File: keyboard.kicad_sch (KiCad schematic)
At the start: 273 parts, among them J3 USB_C_Receptacle_USB2.0, Q1 DTC143Z, SW1 SW_Push, U1 MIC5219-3.3YMM, U3 STM32F072R8Tx, Y1 16MHz

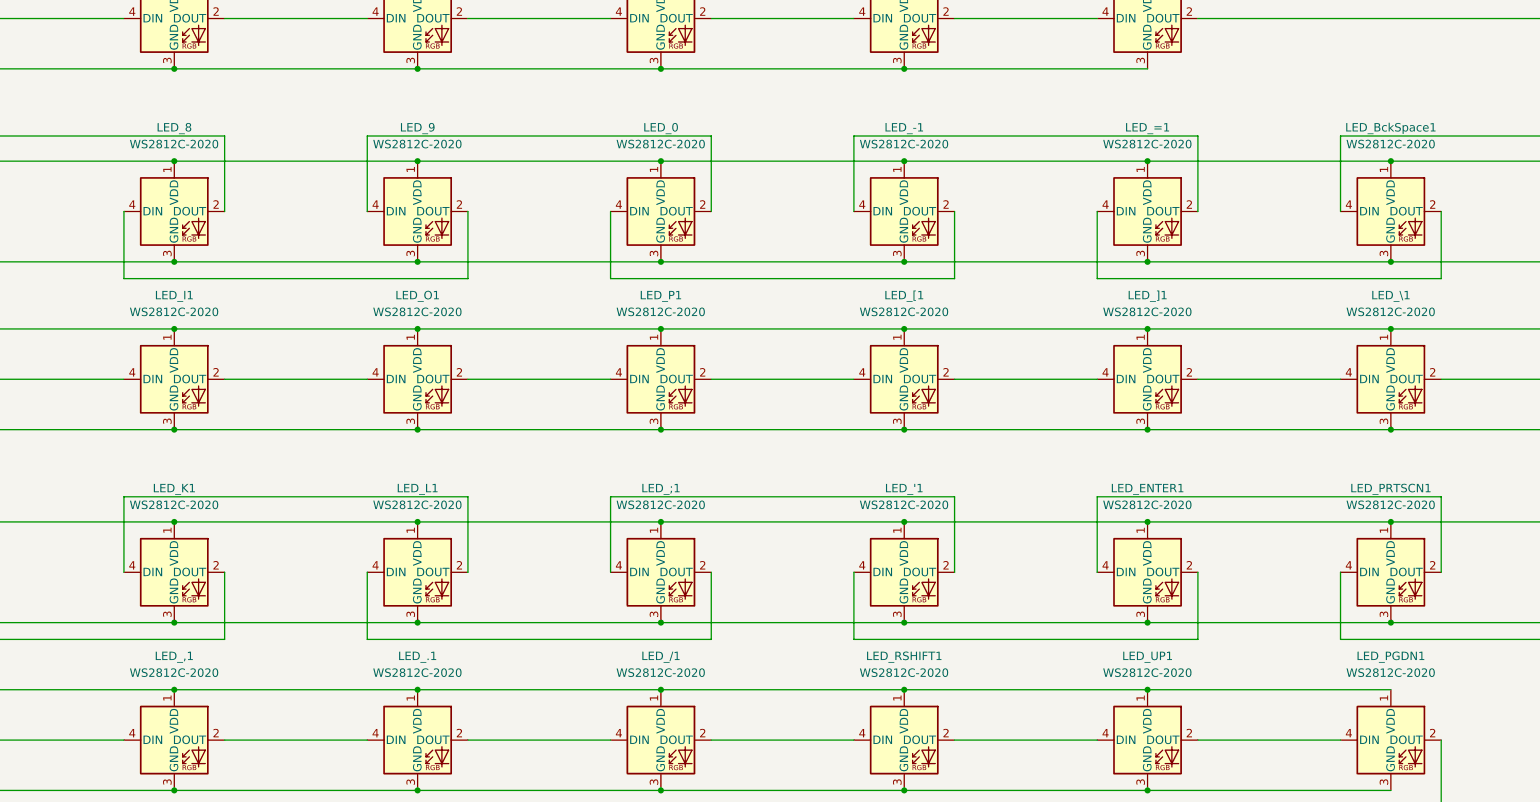
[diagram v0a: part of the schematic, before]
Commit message: fixed led for minus with custom footprint
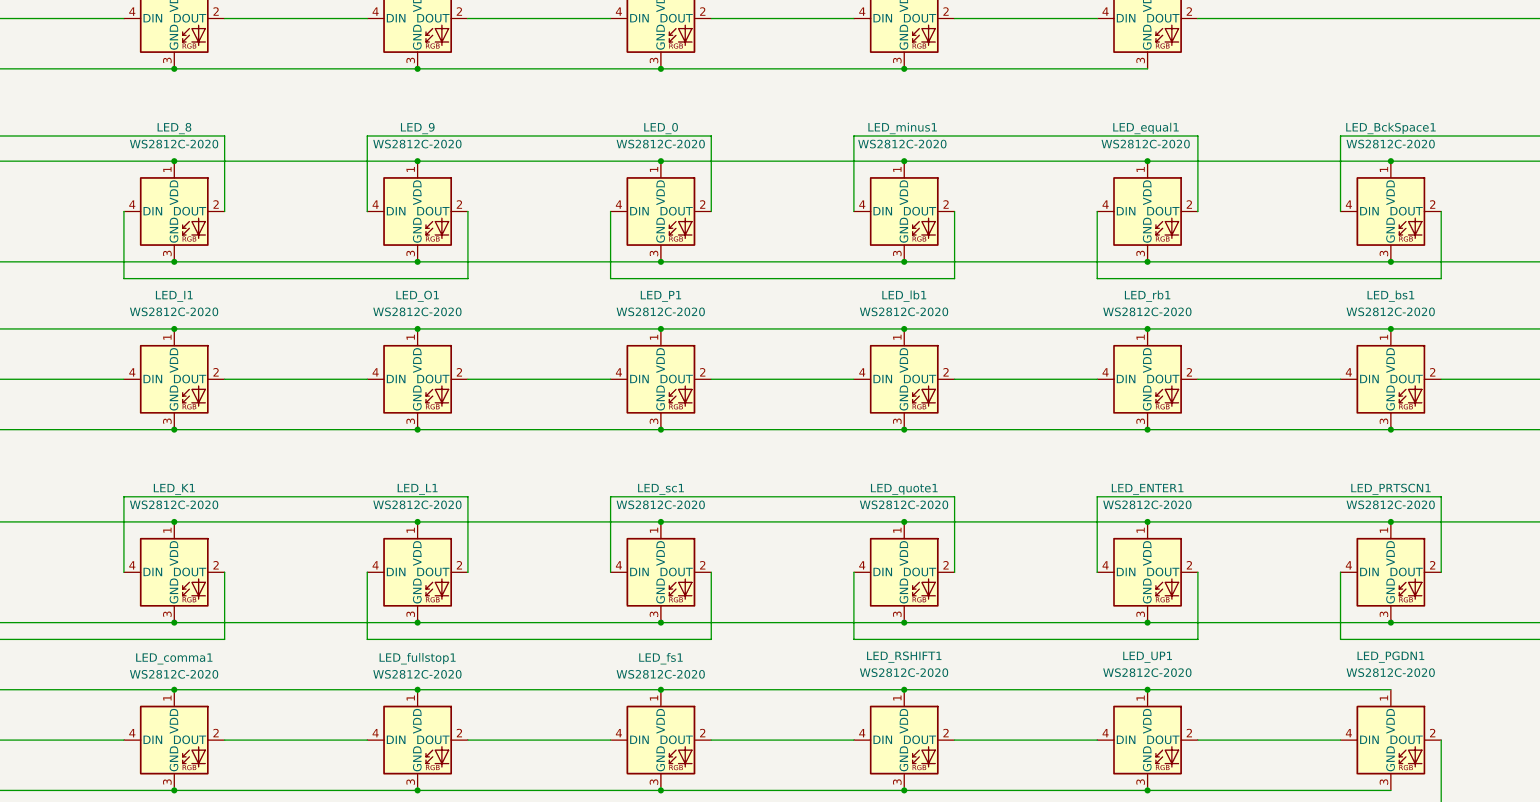
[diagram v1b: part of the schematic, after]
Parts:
- renumbered LED_\1 to LED_bs1, LED_,1 to LED_comma1, LED_=1 to LED_equal1, LED_/1 to LED_fs1, LED_.1 to LED_fullstop1, LED_[1 to LED_lb1, LED_-1 to LED_minus1, LED_'1 to LED_quote1, LED_]1 to LED_rb1, LED_;1 to LED_sc1
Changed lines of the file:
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@@
 		(on_board yes)
 		(dnp no)
-		(property "Reference" "LED_\\1"
+		(property "Reference" "LED_bs1"
 			(at 534.67 321.31 0)
 			(effects
@@
 			(project "pcb-guide"
 				(path "/0abdda29-5dd4-4b90-a349-ef0f202cc9c1"
-					(reference "LED_\\1")
+					(reference "LED_bs1")
 					(unit 1)
 				)
@@
 		(on_board yes)
 		(dnp no)
-		(fields_autoplaced yes)
-		(property "Reference" "LED_-1"
-			(at 461.01 295.91 0)
+		(property "Reference" "LED_minus1"
+			(at 460.756 295.91 0)
 			(effects
 				(font
@@
 		)
 		(property "Value" "WS2812C-2020"
-			(at 461.01 298.45 0)
+			(at 460.756 298.45 0)
 			(effects
 				(font
@@
 			(project "pcb-guide"
 				(path "/0abdda29-5dd4-4b90-a349-ef0f202cc9c1"
-					(reference "LED_-1")
+					(reference "LED_minus1")
 					(unit 1)
 				)
@@
 		(on_board yes)
 		(dnp no)
-		(fields_autoplaced yes)
-		(property "Reference" "LED_'1"
+		(property "Reference" "LED_quote1"
 			(at 461.01 350.52 0)
 			(effects
@@
 			(project "pcb-guide"
 				(path "/0abdda29-5dd4-4b90-a349-ef0f202cc9c1"
-					(reference "LED_'1")
+					(reference "LED_quote1")
 					(unit 1)
 				)
@@
 		(on_board yes)
 		(dnp no)
-		(fields_autoplaced yes)
-		(property "Reference" "LED_;1"
+		(property "Reference" "LED_sc1"
 			(at 424.18 350.52 0)
 			(effects
@@
 			(project "pcb-guide"
 				(path "/0abdda29-5dd4-4b90-a349-ef0f202cc9c1"
-					(reference "LED_;1")
+					(reference "LED_sc1")
 					(unit 1)
 				)
@@
 		(on_board yes)
 		(dnp no)
-		(property "Reference" "LED_]1"
+		(property "Reference" "LED_rb1"
 			(at 497.84 321.31 0)
 			(effects
@@
 			(project "pcb-guide"
 				(path "/0abdda29-5dd4-4b90-a349-ef0f202cc9c1"
-					(reference "LED_]1")
+					(reference "LED_rb1")
 					(unit 1)
 				)
@@
 		(on_board yes)
 		(dnp no)
-		(fields_autoplaced yes)
-		(property "Reference" "LED_/1"
-			(at 424.18 375.92 0)
+		(property "Reference" "LED_fs1"
+			(at 424.18 376.174 0)
 			(effects
 				(font
@@
 		)
 		(property "Value" "WS2812C-2020"
-			(at 424.18 378.46 0)
+			(at 424.18 378.714 0)
 			(effects
 				(font
@@
 			(project "pcb-guide"
 				(path "/0abdda29-5dd4-4b90-a349-ef0f202cc9c1"
-					(reference "LED_/1")
+					(reference "LED_fs1")
 					(unit 1)
 				)
@@
 		(on_board yes)
 		(dnp no)
-		(fields_autoplaced yes)
-		(property "Reference" "LED_=1"
-			(at 497.84 295.91 0)
+		(property "Reference" "LED_equal1"
+			(at 497.586 295.91 0)
 			(effects
 				(font
@@
 		)
 		(property "Value" "WS2812C-2020"
-			(at 497.84 298.45 0)
+			(at 497.586 298.45 0)
 			(effects
 				(font
@@
 			(project "pcb-guide"
 				(path "/0abdda29-5dd4-4b90-a349-ef0f202cc9c1"
-					(reference "LED_=1")
+					(reference "LED_equal1")
 					(unit 1)
 				)
@@
 		(on_board yes)
 		(dnp no)
-		(property "Reference" "LED_[1"
+		(property "Reference" "LED_lb1"
 			(at 461.01 321.31 0)
 			(effects
@@
 			(project "pcb-guide"
 				(path "/0abdda29-5dd4-4b90-a349-ef0f202cc9c1"
-					(reference "LED_[1")
+					(reference "LED_lb1")
 					(unit 1)
 				)
@@
 		(on_board yes)
 		(dnp no)
-		(fields_autoplaced yes)
-		(property "Reference" "LED_.1"
-			(at 387.35 375.92 0)
+		(property "Reference" "LED_fullstop1"
+			(at 387.35 376.174 0)
 			(effects
 				(font
@@
 		)
 		(property "Value" "WS2812C-2020"
-			(at 387.35 378.46 0)
+			(at 387.35 378.714 0)
 			(effects
 				(font
@@
 			(project "pcb-guide"
 				(path "/0abdda29-5dd4-4b90-a349-ef0f202cc9c1"
-					(reference "LED_.1")
+					(reference "LED_fullstop1")
 					(unit 1)
 				)
@@
 		(on_board yes)
 		(dnp no)
-		(fields_autoplaced yes)
-		(property "Reference" "LED_,1"
-			(at 350.52 375.92 0)
+		(property "Reference" "LED_comma1"
+			(at 350.52 376.174 0)
 			(effects
 				(font
@@
 		)
 		(property "Value" "WS2812C-2020"
-			(at 350.52 378.46 0)
+			(at 350.52 378.714 0)
 			(effects
 				(font
@@
 			(project "pcb-guide"
 				(path "/0abdda29-5dd4-4b90-a349-ef0f202cc9c1"
-					(reference "LED_,1")
+					(reference "LED_comma1")
 					(unit 1)
 				)

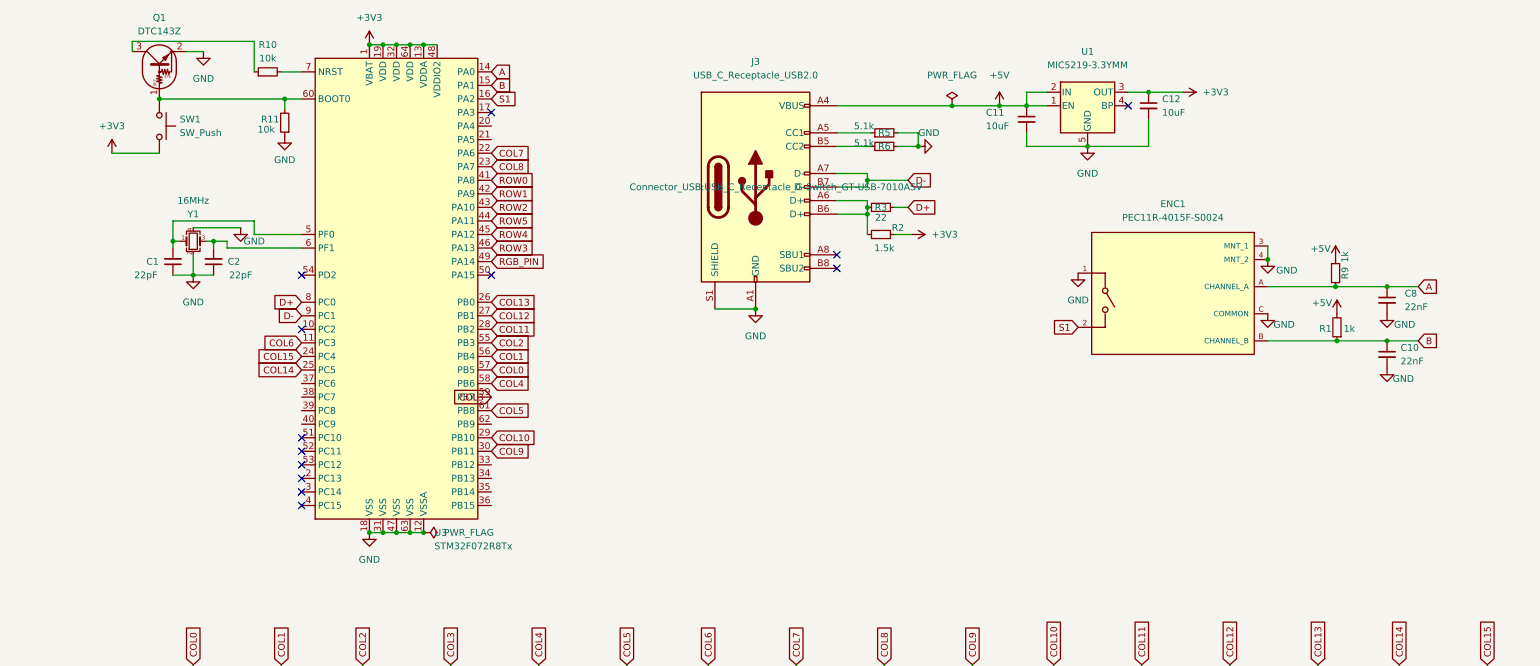
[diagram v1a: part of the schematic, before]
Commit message: Updated footprints, still need to do usb
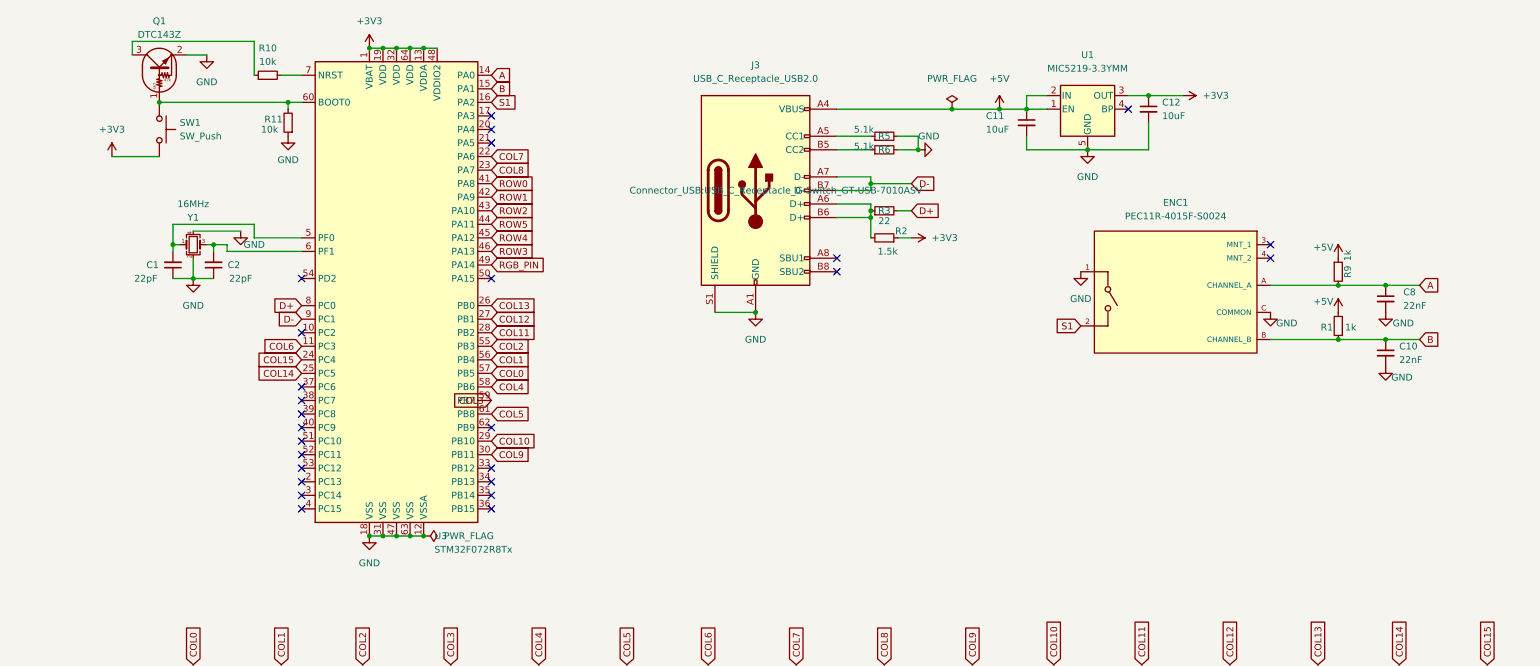
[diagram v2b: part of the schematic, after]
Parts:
- ENC1: footprint Bourns-PEC11R-4015F-S0024-* -> encoder:XDCR_PEC11R-4215F-S0024
- LED_0, LED_1, LED_2, LED_3, LED_4, LED_5, LED_6, LED_7, LED_8, LED_9, LED_A1, LED_B1, LED_BckSpace1, LED_C1, LED_CAPS1, LED_D1, LED_DOWN1, LED_Del1, LED_E1, LED_ENTER1, LED_End1, LED_Esc1, LED_F1, LED_F10, LED_F11, LED_F12, LED_F13, LED_F2, LED_F3, LED_F4, LED_F5, LED_F6, LED_F7, LED_F8, LED_F9, LED_G1, LED_H1, LED_Home1, LED_I1, LED_Ins1, LED_J1, LED_K1, LED_L1, LED_LALT1, LED_LCTRL1, LED_LEFT1, LED_LSHIFT1, LED_LWIN1, LED_M1, LED_N1, LED_O1, LED_P1, LED_PGDN1, LED_PGUP1, LED_PRTSCN1, LED_Q1, LED_R1, LED_RALT1, LED_RCTRL1, LED_RIGHT1, LED_RSHIFT1, LED_RWIN1, LED_S1, LED_SPACE1, LED_T1, LED_TAB1, LED_Tilda1, LED_U1, LED_UP1, LED_V1, LED_W1, LED_X1, LED_Y1, LED_Z1, LED_bs1, LED_comma1, LED_equal1, LED_fs1, LED_fullstop1, LED_lb1, LED_minus1, LED_quote1, LED_rb1, LED_sc1: footprint Keebio-Parts:SK6812-MINI-E -> keebio-Parts:SK6812-MINI-E-CUSTOM
- MX_'1, MX_,1, MX_-1, MX_.1, MX_/1, MX_0, MX_1, MX_2, MX_3, MX_4, MX_5, MX_7, MX_8, MX_9, MX_;1, MX_=1, MX_A1, MX_B1, MX_C1, MX_D1, MX_Del1, MX_Down1, MX_E1, MX_End1, MX_Esc1, MX_F1, MX_F10, MX_F11, MX_F12, MX_F13, MX_F2, MX_F3, MX_F4, MX_F5, MX_F6, MX_F7, MX_F8, MX_F9, MX_G1, MX_H1, MX_Home1, MX_I1, MX_Ins1, MX_J1, MX_K1, MX_L1, MX_Left1, MX_M1, MX_N1, MX_O1, MX_P1, MX_PgDn1, MX_PgUp1, MX_PtrSc1, MX_Q1, MX_R1, MX_Right1, MX_S1, MX_T1, MX_Tilda1, MX_U1, MX_Up1, MX_V1, MX_W1, MX_X1, MX_Y1, MX_Z1, MX_[1, MX_]1: footprint MX_Alps_Hybrid:MX-1U-NoLED -> PCM_Switch_Keyboard_Cherry_MX:SW_Cherry_MX_PCB_1.00u
- MX_6: footprint pcb-guide:MX-1U-NoLED -> PCM_Switch_Keyboard_Cherry_MX:SW_Cherry_MX_PCB_1.00u
- MX_BckSpace1: footprint MX_Alps_Hybrid:MX-2U-NoLED -> PCM_Switch_Keyboard_Cherry_MX:Cherry 2u with stablizer
- MX_Caps1: footprint MX_Alps_Hybrid:MX-1.75U-NoLED -> PCM_Switch_Keyboard_Cherry_MX:SW_Cherry_MX_PCB_1.75u
- MX_Enter1, MX_LShift1: footprint MX_Alps_Hybrid:MX-2.25U-NoLED -> PCM_Switch_Keyboard_Cherry_MX:Cherry 2.25 with stablizer
- MX_LAlt1, MX_LCtrl1, MX_LWin1, MX_RAlt1, MX_RCtrl1, MX_RWin1: footprint MX_Alps_Hybrid:MX-1.25U-NoLED -> PCM_Switch_Keyboard_Cherry_MX:SW_Cherry_MX_PCB_1.25u
- MX_RShift1: footprint MX_Alps_Hybrid:MX-2.75U-NoLED -> PCM_Switch_Keyboard_Cherry_MX:Cherry 2.75 with stablizer
- MX_Space1: footprint MX_Alps_Hybrid:MX-6U-Centered-NoLED -> PCM_Switch_Keyboard_Cherry_MX:Cherry 6u with upside down Stablizer
- MX_Tab1, MX_\1: footprint MX_Alps_Hybrid:MX-1.5U-NoLED -> PCM_Switch_Keyboard_Cherry_MX:SW_Cherry_MX_PCB_1.50u
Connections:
- net GND: no longer ENC1.3 (MNT_1), ENC1.4 (MNT_2)
- no-connect marks 14 -> 27
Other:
- moved on the sheet: C1, C11, C12, C2, ENC1, J3, Q1, R10, R11, R2, R3, R5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

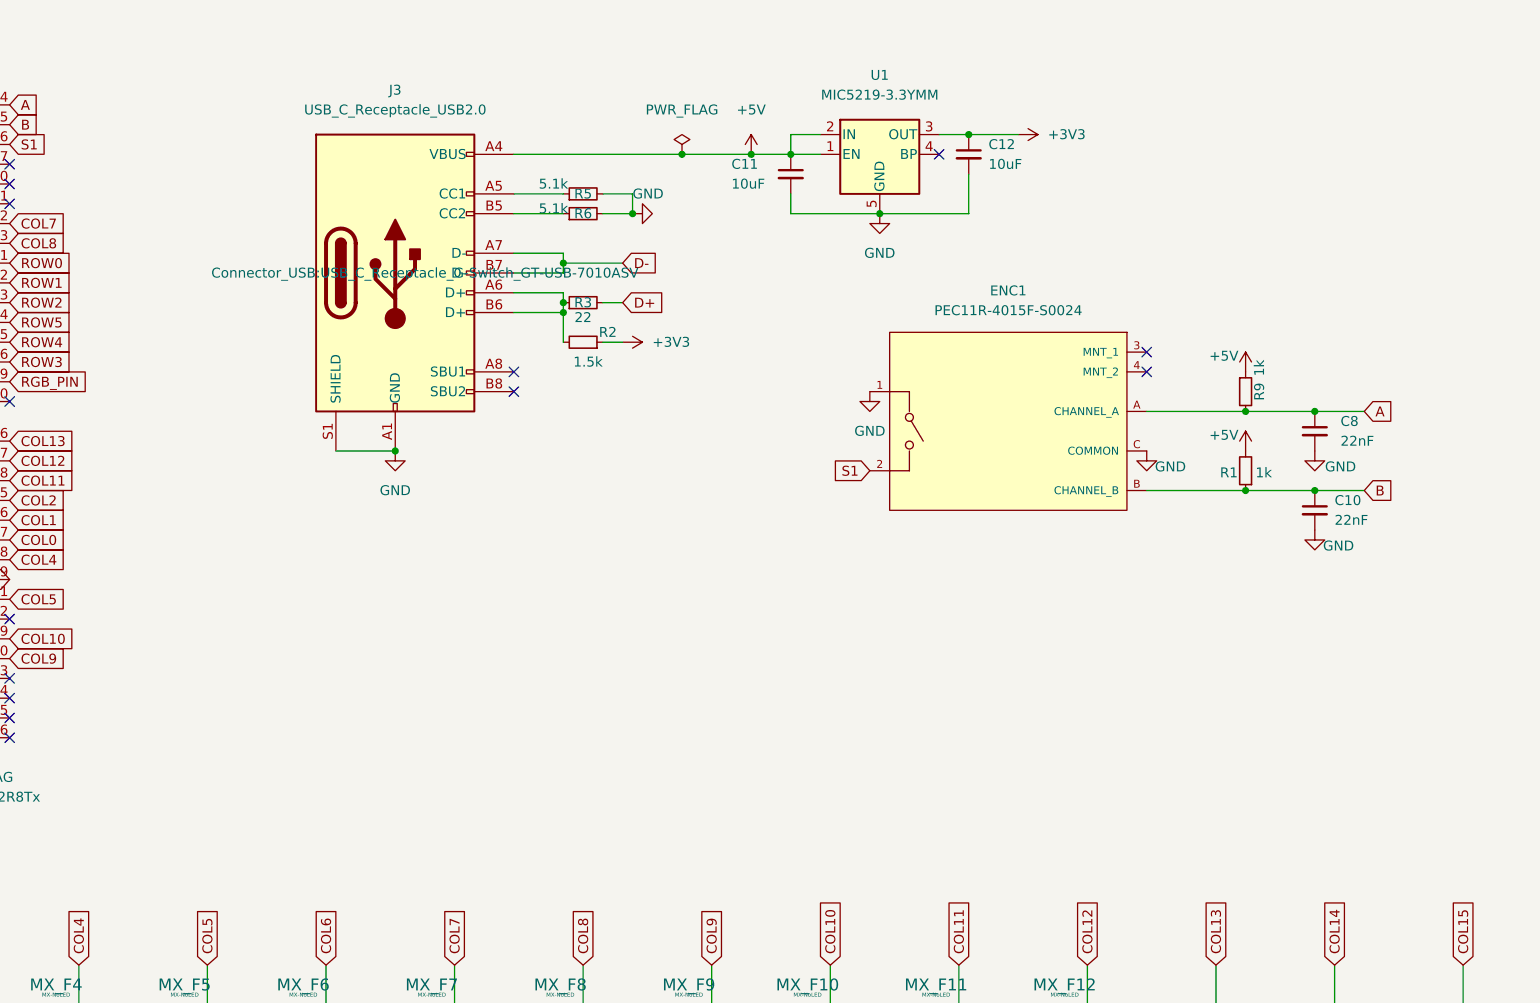
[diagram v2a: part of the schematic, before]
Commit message: Updated usbc,moved leds,added gnd zone,fixed some routing
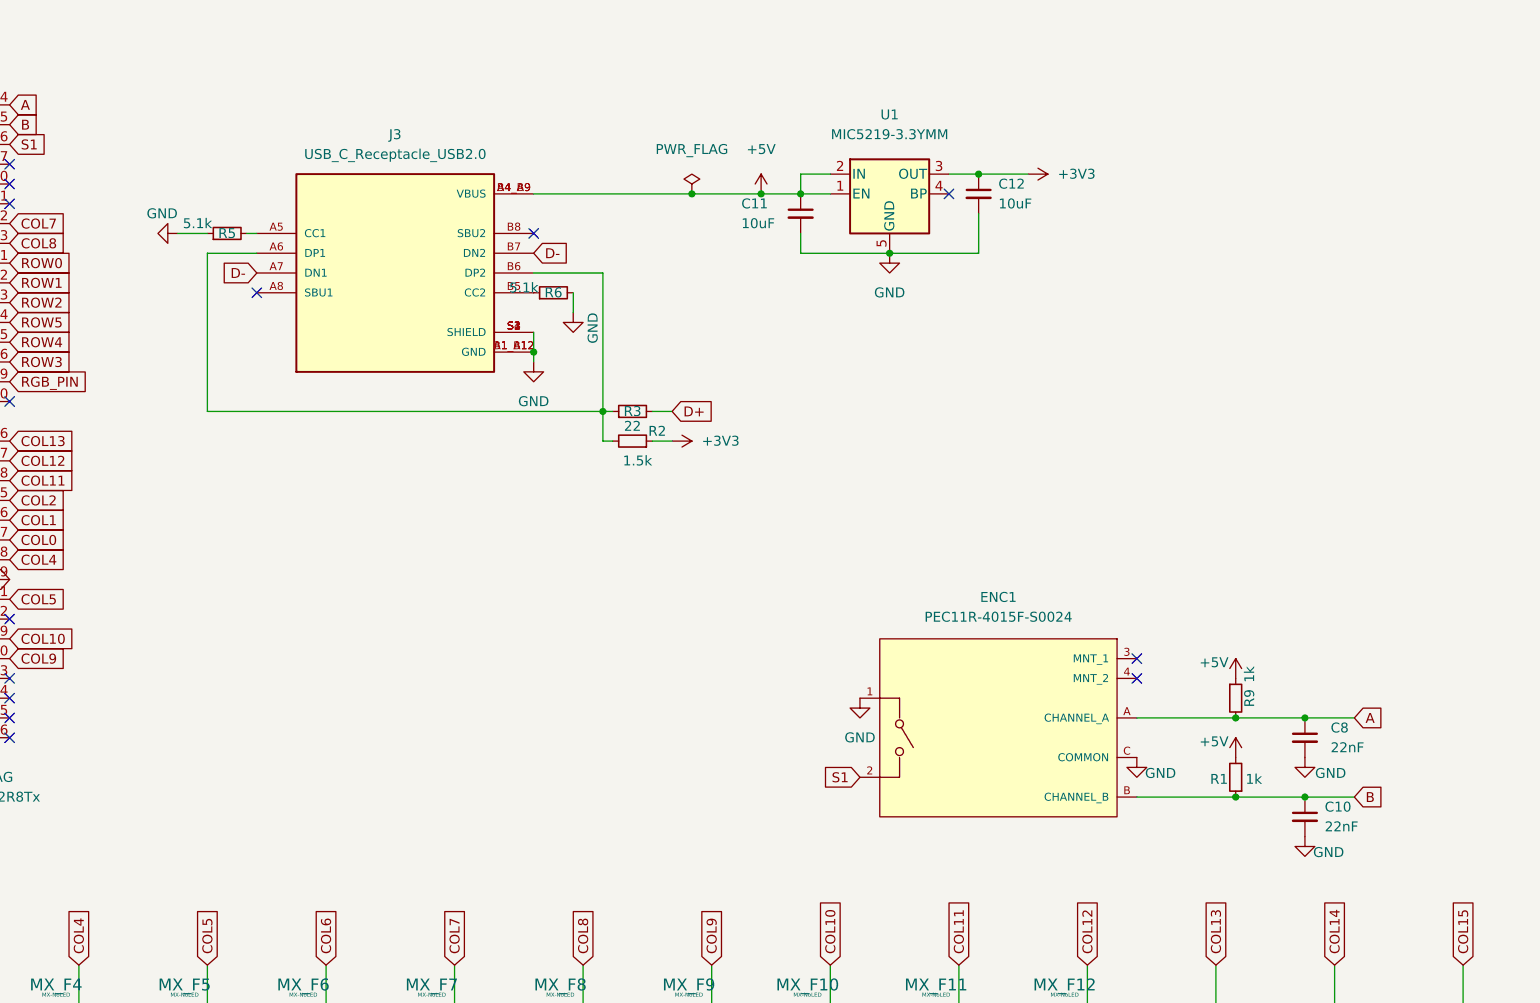
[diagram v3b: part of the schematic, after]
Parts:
- J3: footprint Connector_USB:USB_C_Receptacle_G-Switch_GT-USB-7010ASV -> TYPE-C-31-M-12:HRO_TYPE-C-31-M-12; symbol Connector:USB_C_Receptacle_USB2.0 -> USB_C:TYPE-C-31-M-12; Availability (none) -> Not in stock; Check_prices (none) -> https://www.snapeda.com/parts/TYPE-C-31-M-12/HRO+Electronic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; Description_1 (none) -> USB Connectors 24 Receptacle 1 8.94*7.3mm RoHS; MANUFACTURER (none) -> HRO Electronics Co., Ltd.; MAXIMUM_PACKAGE_HEIGHT (none) -> 3.26 mm; MF (none) -> HRO Electronics Co., Ltd.; MP (none) -> TYPE-C-31-M-12; PARTREV (none) -> 2020.12.08; Package (none) -> Package; Price (none) -> None; SNAPEDA_PN (none) -> TYPE-C-31-M-12; STANDARD (none) -> Manufacturer Recommendations; SnapEDA_Link (none) -> https://www.snapeda.com/parts/TYPE-C-31-M-12/HRO+Electronic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
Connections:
- net +5V: now also J3.A4_B9 (VBUS), J3.B4_A9 (VBUS); no longer J3.A4 (VBUS), J3.A9 (VBUS), J3.B4 (VBUS), J3.B9 (VBUS)
- net GND: now also J3.A1_B12 (GND), J3.B1_A12 (GND), J3.S2 (SHIELD), J3.S3 (SHIELD), J3.S4 (SHIELD), R5.1; no longer J3.A1 (GND), J3.A12 (GND), J3.B1 (GND), J3.B12 (GND), R5.2
- net at J3.A5 (CC1): now also R5.2; no longer R5.1
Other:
- moved on the sheet: C10, C11, C12, C8, ENC1, R1, R2, R3, R5, R6, R9, U1
